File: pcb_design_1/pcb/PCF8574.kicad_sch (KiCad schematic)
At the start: 13 parts, among them SW2 SW_Push, SW3 SW_Push, SW4 SW_Push, SW5 SW_Push, U1 PCF8574TS

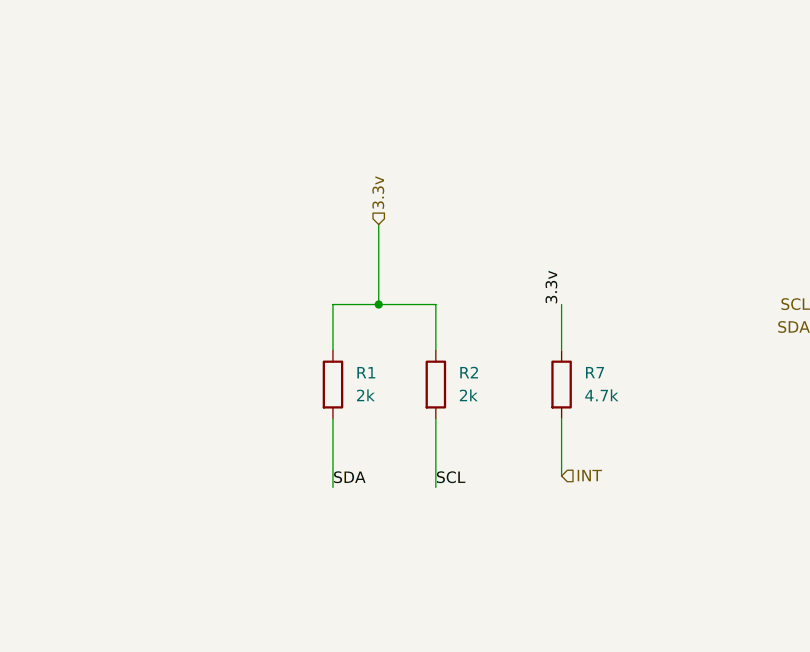
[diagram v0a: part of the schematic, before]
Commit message: Add TOF sensor sheet and move I2C resistors
- Created new Sensors_TOF schematic sheet for Time-of-Flight sensor with I2C interface
- Moved I2C pull-up resistors (R8, R9, 2k ohm) from PCF8574 to ESP32 sheet
- Added hierarchical labels (SDA, SCL, 3.3v) to ESP32 sheet for I2C connectivity
- Added TOF sensor connector (J7) with 6-pin socket connection
- Updated project designators in pcb.kicad_pro
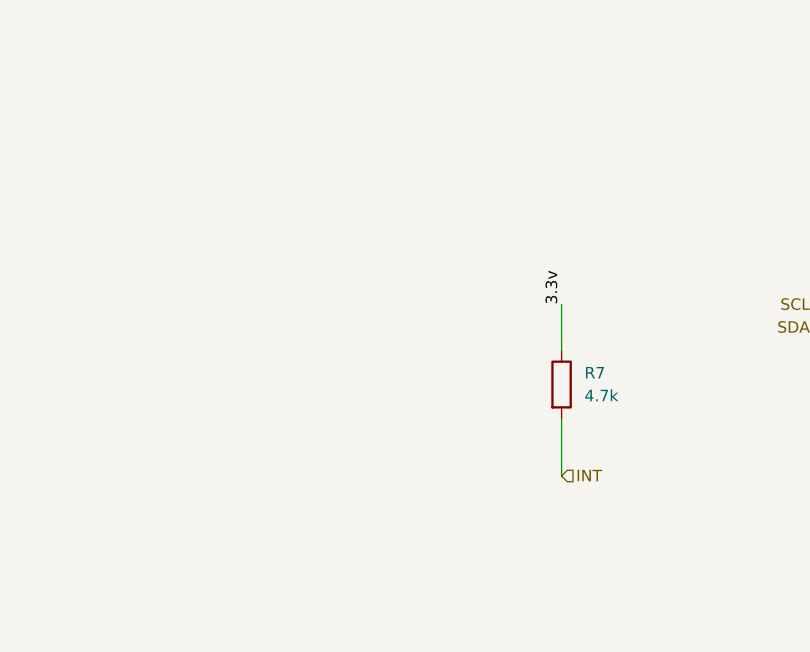
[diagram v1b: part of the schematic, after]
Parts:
- removed R1, R2: 2k, symbol Device:R

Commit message: improved the designed
improved the designed
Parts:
- removed D1: LED_RGBK, symbol Device:LED_RGBK
- removed LS1: KPEG242-5V, KPEG242-5V:XDCR_KPEG242-5V, symbol KPEG242-5V:KPEG242-5V
- removed R4, R5, R6: R, symbol Device:R
- removed SW2, SW3, SW4, SW5: SW_Push, symbol Switch:SW_Push
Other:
- added sheet Speker (Speker.kicad_sch)
- added sheet Switches (Switches.kicad_sch)
- added sheet indication_circuit (indication_circuit.kicad_sch)
- moved on the sheet: R7, U1
